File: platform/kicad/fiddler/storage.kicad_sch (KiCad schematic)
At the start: 2 parts, among them J1 5033981892

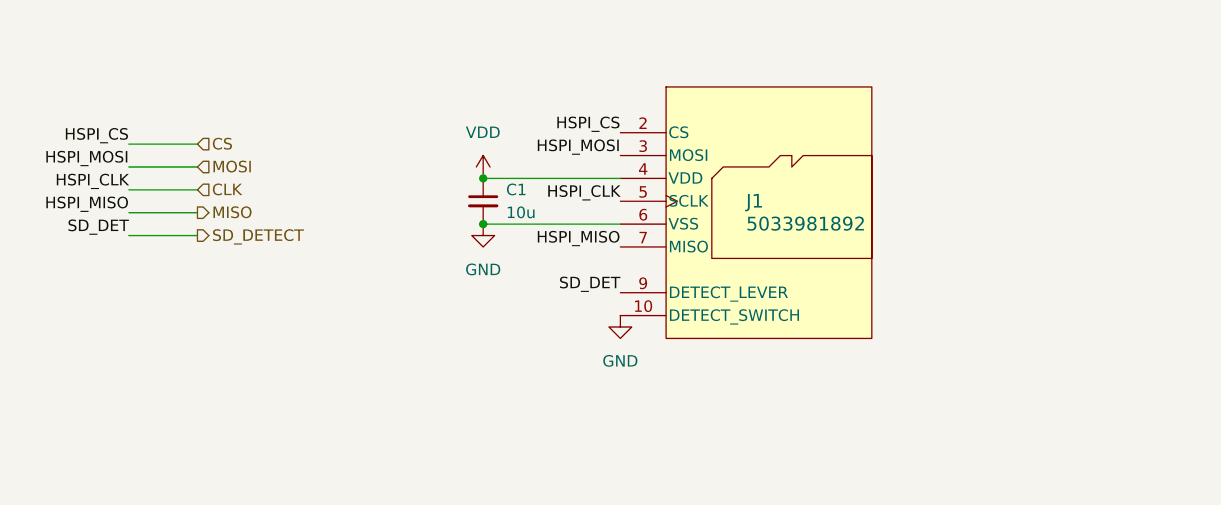
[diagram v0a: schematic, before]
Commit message: Fiddler Ray Speaker: Complete first revision
This change completes the first iteration schematic and layout for the fiddler ray speaker PCB.
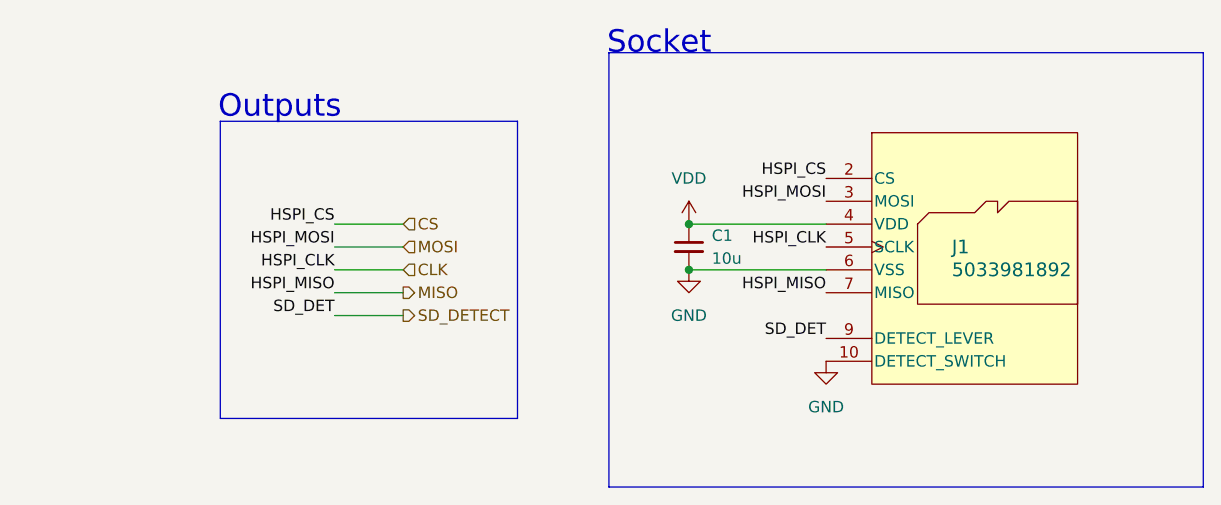
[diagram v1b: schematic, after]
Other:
- note added: "Outputs"
- note added: "Socket"
- company: (none) -> The Australian Ocean Laboratory
- title: (none) -> Fiddler Ray Speaker Unit V1
- moved on the sheet: C1, J1

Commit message: Fiddler Ray Speaker: Production rev A
This change adds additional data to components to populate SPN for
the BOM via JLC
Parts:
- C1: LCSC Part # (none) -> C19702
- J1: LCSC Part # (none) -> C428492
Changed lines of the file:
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@@
+			)
+		)
+		(property "Voltage Rating" ""
+			(at 151.13 95.25 0)
+			(effects
+				(font
+					(size 1.27 1.27)
+				)
+				(hide yes)
+			)
+		)
+		(property "LCSC Part #" "C19702"
+			(at 151.13 95.25 0)
+			(effects
+				(font
+					(size 1.27 1.27)
+				)
+				(hide yes)
 			)
 		)
@@
 			(at 166.37 85.09 0)
 			(effects
+				(font
+					(size 1.27 1.27)
+				)
+				(hide yes)
+			)
+		)
+		(property "Voltage Rating" ""
+			(at 166.37 85.09 0)
+			(effects
+				(font
+					(size 1.27 1.27)
+				)
+				(hide yes)
+			)
+		)
+		(property "LCSC Part #" "C428492"
+			(at 166.37 85.09 0)
+			(effects
